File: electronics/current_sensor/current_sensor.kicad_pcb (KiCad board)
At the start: 2 copper layers, 20 parts, among them J1 CS connector, J2 External connector, U1 INA253A3IPWR, U2 AD7685CRMZ, U3 ADR435BRMZ, U4 ADP7104ARDZ-5.0-R7, U5 ADP7104ARDZ-9.0-R7

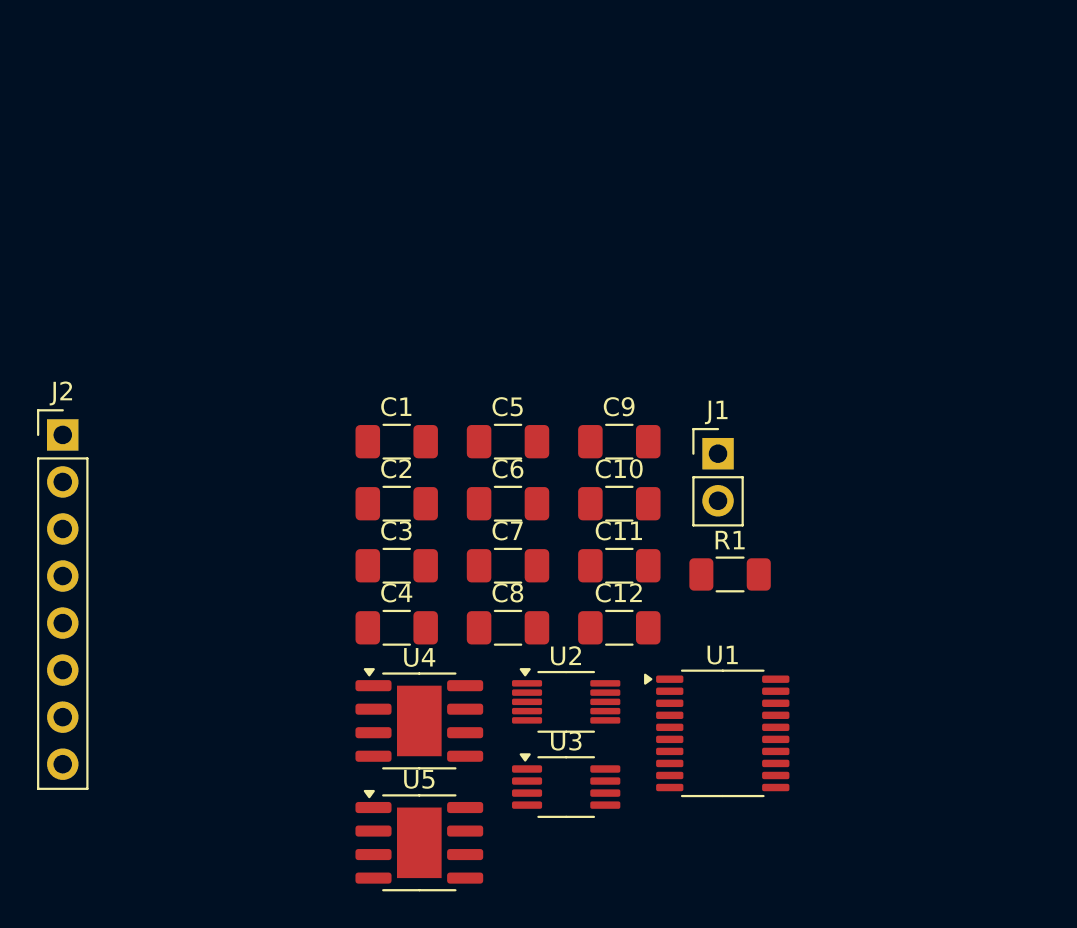
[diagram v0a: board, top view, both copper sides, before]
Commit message: Update - Need to improve Storage class, very messy
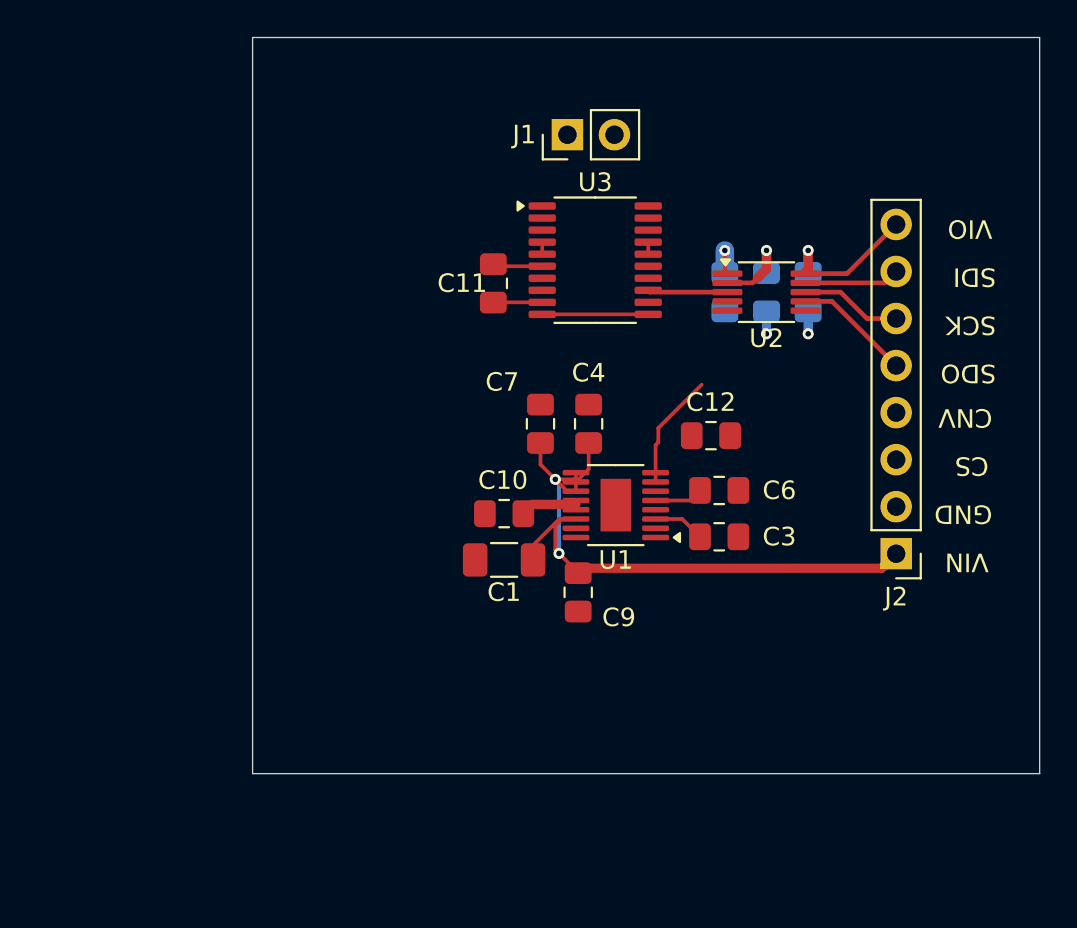
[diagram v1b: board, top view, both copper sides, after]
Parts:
- removed R1: 82k, Resistor_SMD:R_1206_3216Metric_Pad1.30x1.75mm_HandSolder
- removed the U3 at (120.2, 84.5)
- removed U4: ADP7104ARDZ-5.0-R7, Package_SO:SOIC-8-1EP_3.9x4.9mm_P1.27mm_EP2.41x3.81mm
- removed U5: ADP7104ARDZ-9.0-R7, Package_SO:SOIC-8-1EP_3.9x4.9mm_P1.27mm_EP2.41x3.81mm
- added U1: LT6658AHMSE-5#PBF, Package_SO:MSOP-16-1EP_3x4.039mm_P0.5mm_EP1.651x2.845mm, F.Cu at (122.9, 69.2)
- C1: value 100nF -> 1uF
- C10, C12, C7: footprint Capacitor_SMD:C_1206_3216Metric_Pad1.33x1.80mm_HandSolder -> Capacitor_SMD:C_0805_2012Metric_Pad1.18x1.45mm_HandSolder
- C11, C9: value 1uF -> 100nF; footprint Capacitor_SMD:C_1206_3216Metric_Pad1.33x1.80mm_HandSolder -> Capacitor_SMD:C_0805_2012Metric_Pad1.18x1.45mm_HandSolder
- C2, C8: footprint Capacitor_SMD:C_1206_3216Metric_Pad1.33x1.80mm_HandSolder -> Capacitor_SMD:C_0805_2012Metric_Pad1.18x1.45mm_HandSolder; moved to B.Cu
- C3: value 100nF -> 1uF; footprint Capacitor_SMD:C_1206_3216Metric_Pad1.33x1.80mm_HandSolder -> Capacitor_SMD:C_0805_2012Metric_Pad1.18x1.45mm_HandSolder
- C4: value 22uF -> 100nF; footprint Capacitor_SMD:C_1206_3216Metric_Pad1.33x1.80mm_HandSolder -> Capacitor_SMD:C_0805_2012Metric_Pad1.18x1.45mm_HandSolder
- C5: value 10nF -> 10uF; footprint Capacitor_SMD:C_1206_3216Metric_Pad1.33x1.80mm_HandSolder -> Capacitor_SMD:C_0805_2012Metric_Pad1.18x1.45mm_HandSolder; moved to B.Cu
- C6: value 10uF -> 1uF; footprint Capacitor_SMD:C_1206_3216Metric_Pad1.33x1.80mm_HandSolder -> Capacitor_SMD:C_0805_2012Metric_Pad1.18x1.45mm_HandSolder
- moved J2 45.5 mm to (138.0, 71.9), turned to 180 degrees
- moved U3 26.5 mm to (121.8, 56.0)
- moved C2 25.0 mm to (133.2, 57.8), turned to -90 degrees
- moved U2 24.6 mm to (131.0, 57.8)
- moved C8 22.9 mm to (131.0, 57.8), turned to -90 degrees
- moved J1 19.0 mm to (120.2, 49.2), turned to 90 degrees
- moved C3 17.5 mm to (128.4, 71.0)
- moved C11 16.7 mm to (116.2, 57.3), turned to 90 degrees
- moved C4 15.1 mm to (121.4, 64.9), turned to 90 degrees
- moved C5 14.2 mm to (128.8, 57.8), turned to -90 degrees
- moved C12 11.5 mm to (128.0, 65.5)
- moved C6 11.4 mm to (128.4, 68.5)
- moved C1 8.63 mm to (116.8, 72.2), turned to 180 degrees
- moved C9 8.43 mm to (120.8, 74.0), turned to -90 degrees
- moved C7 7.86 mm to (118.8, 64.9), turned to 90 degrees
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- renumbered U1 to U3
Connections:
- C1 pad 1: +5V -> /VIN
- C10 pad 1: /SENSE_5 -> +5V
- C11 pad 1: /VIN -> +5V
- C12 pad 1: /SENSE_9 -> /REF
- C2 pad 1: +5V -> /VIO
- C3 pad 1: /VIO -> /BYPASS
- C4 pad 1: /REF -> /VIN
- C5 pad 1: Net-(C5-Pad1) -> /REF
- C5 pad 2: /REF -> GND
- C6 pad 1: +9V -> /NR
- C7 pad 1: +9V -> /VIN
- C8 pad 1: /REF -> +5V
- J2 pad 1: /VIO -> /VIN
- J2 pad 2: /SDI -> GND
- J2 pad 3: /SCK -> /CS
- J2 pad 4: /SDO -> /CNV
- J2 pad 5: /CNV -> /SDO
- J2 pad 6: /VIN -> /SCK
- J2 pad 7: GND -> /SDI
- J2 pad 8: /CS -> /VIO
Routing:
- net /VIN: track 0.00 -> 36.8 mm, vias 0 -> 2
- net +5V: track 0.00 -> 10.8 mm, vias 0 -> 1
- net /REF: track 0.00 -> 8.80 mm, vias 0 -> 1
- net /VIO: track 0.00 -> 8.45 mm, vias 0 -> 1
- net /SDO: track 0.00 -> 6.32 mm
- net Net-(U3-REF1): track 0.00 -> 5.72 mm
- net /SCK: track 0.00 -> 5.48 mm
- net /SDI: track 0.00 -> 5.14 mm
- net GND: track 0.00 -> 4.95 mm, vias 0 -> 2
- net /CS: track 0.00 -> 4.32 mm
- net /BYPASS: track 0.00 -> 2.80 mm
- net /NR: track 0.00 -> 2.62 mm
- net Net-(U3-IN-): track 0.00 -> 0.65 mm
- net Net-(U3-IN+): track 0.00 -> 0.65 mm
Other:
- board outline added: 42.5 x 39.8 mm
- board text added: "CNV"
- board text added: "CS"
- board text added: "GND"
- board text added: "SCK"
- board text added: "SDI"
- board text added: "SDO"
- board text added: "VIN"
- board text added: "VIO"
